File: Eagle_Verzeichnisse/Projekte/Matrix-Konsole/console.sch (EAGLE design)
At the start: 3 parts, among them IC1 74HC595N, IC2 74HC595N

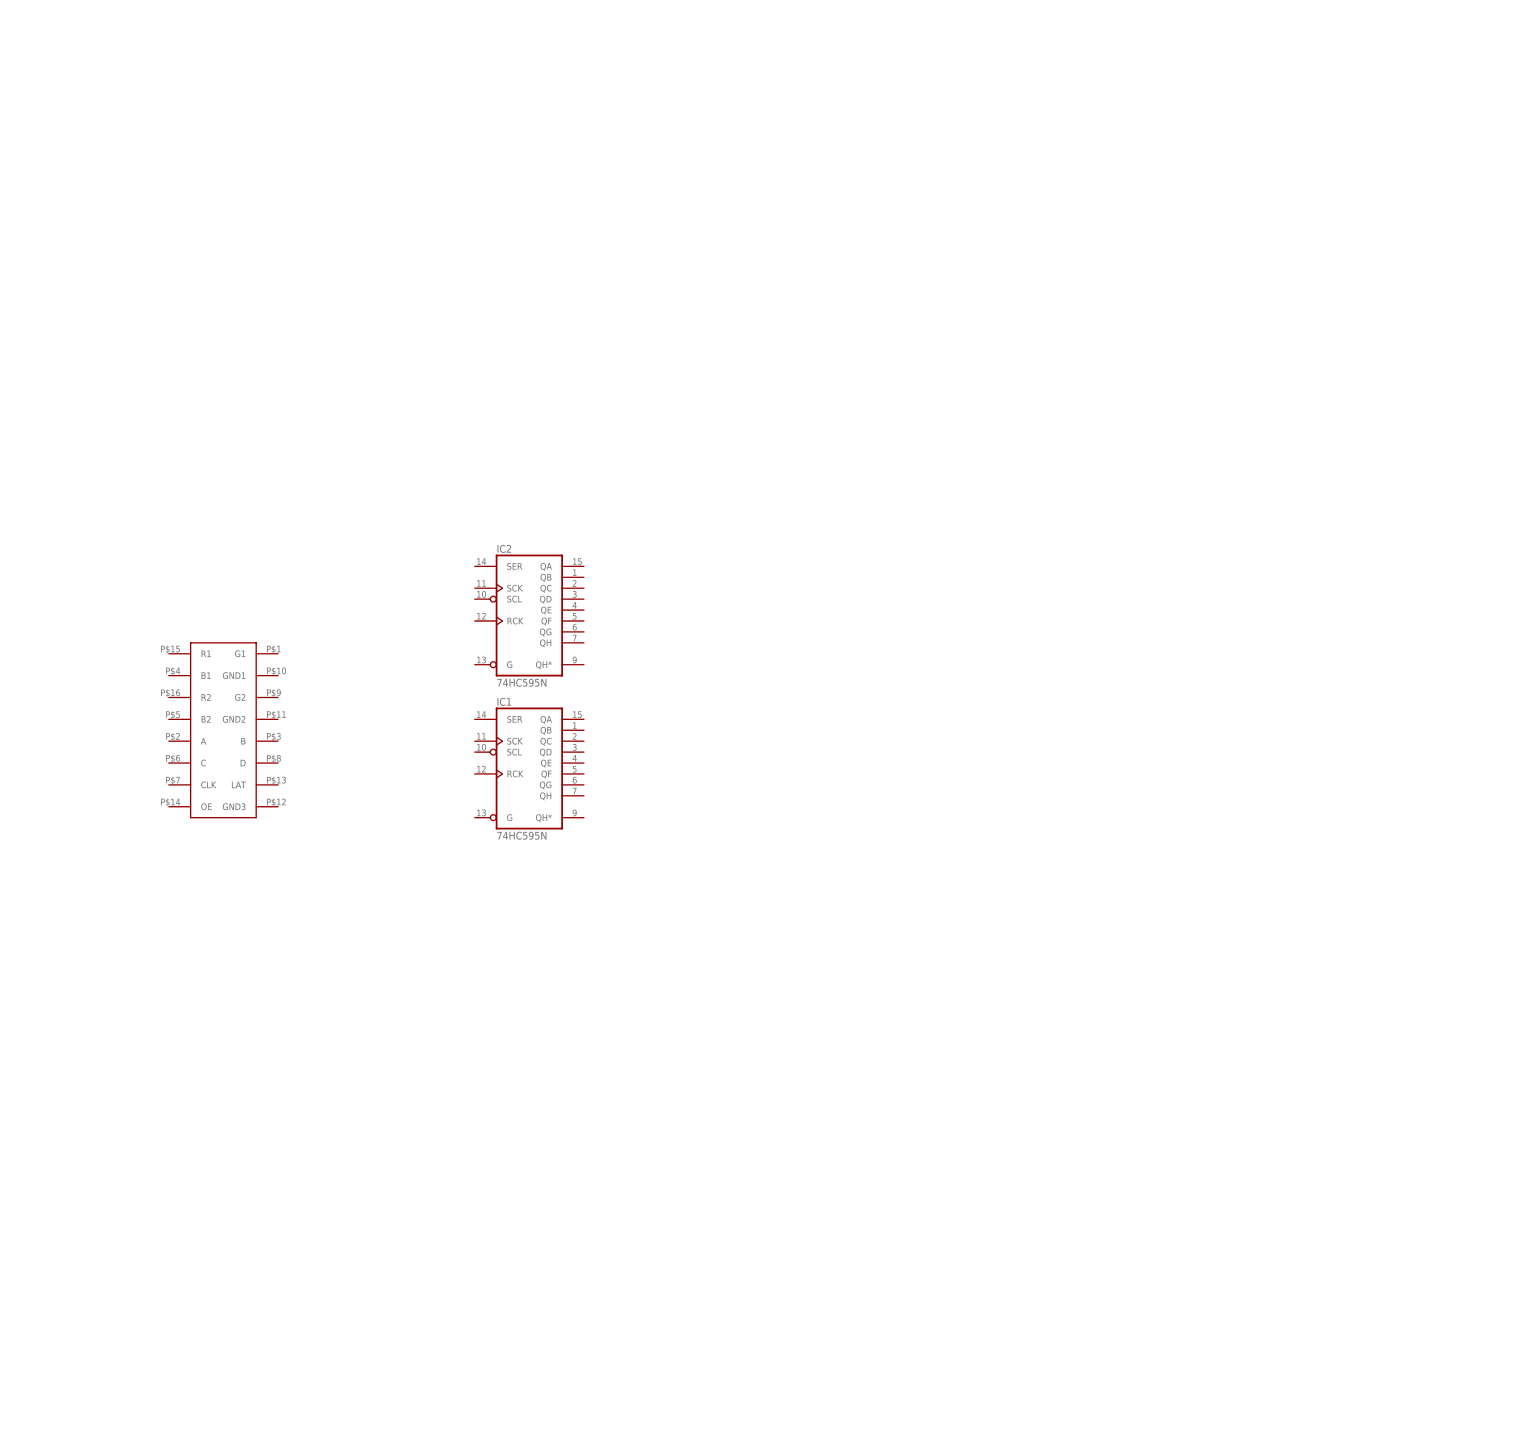
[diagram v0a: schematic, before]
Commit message: Added circuit diagrams, Changed Stückliste
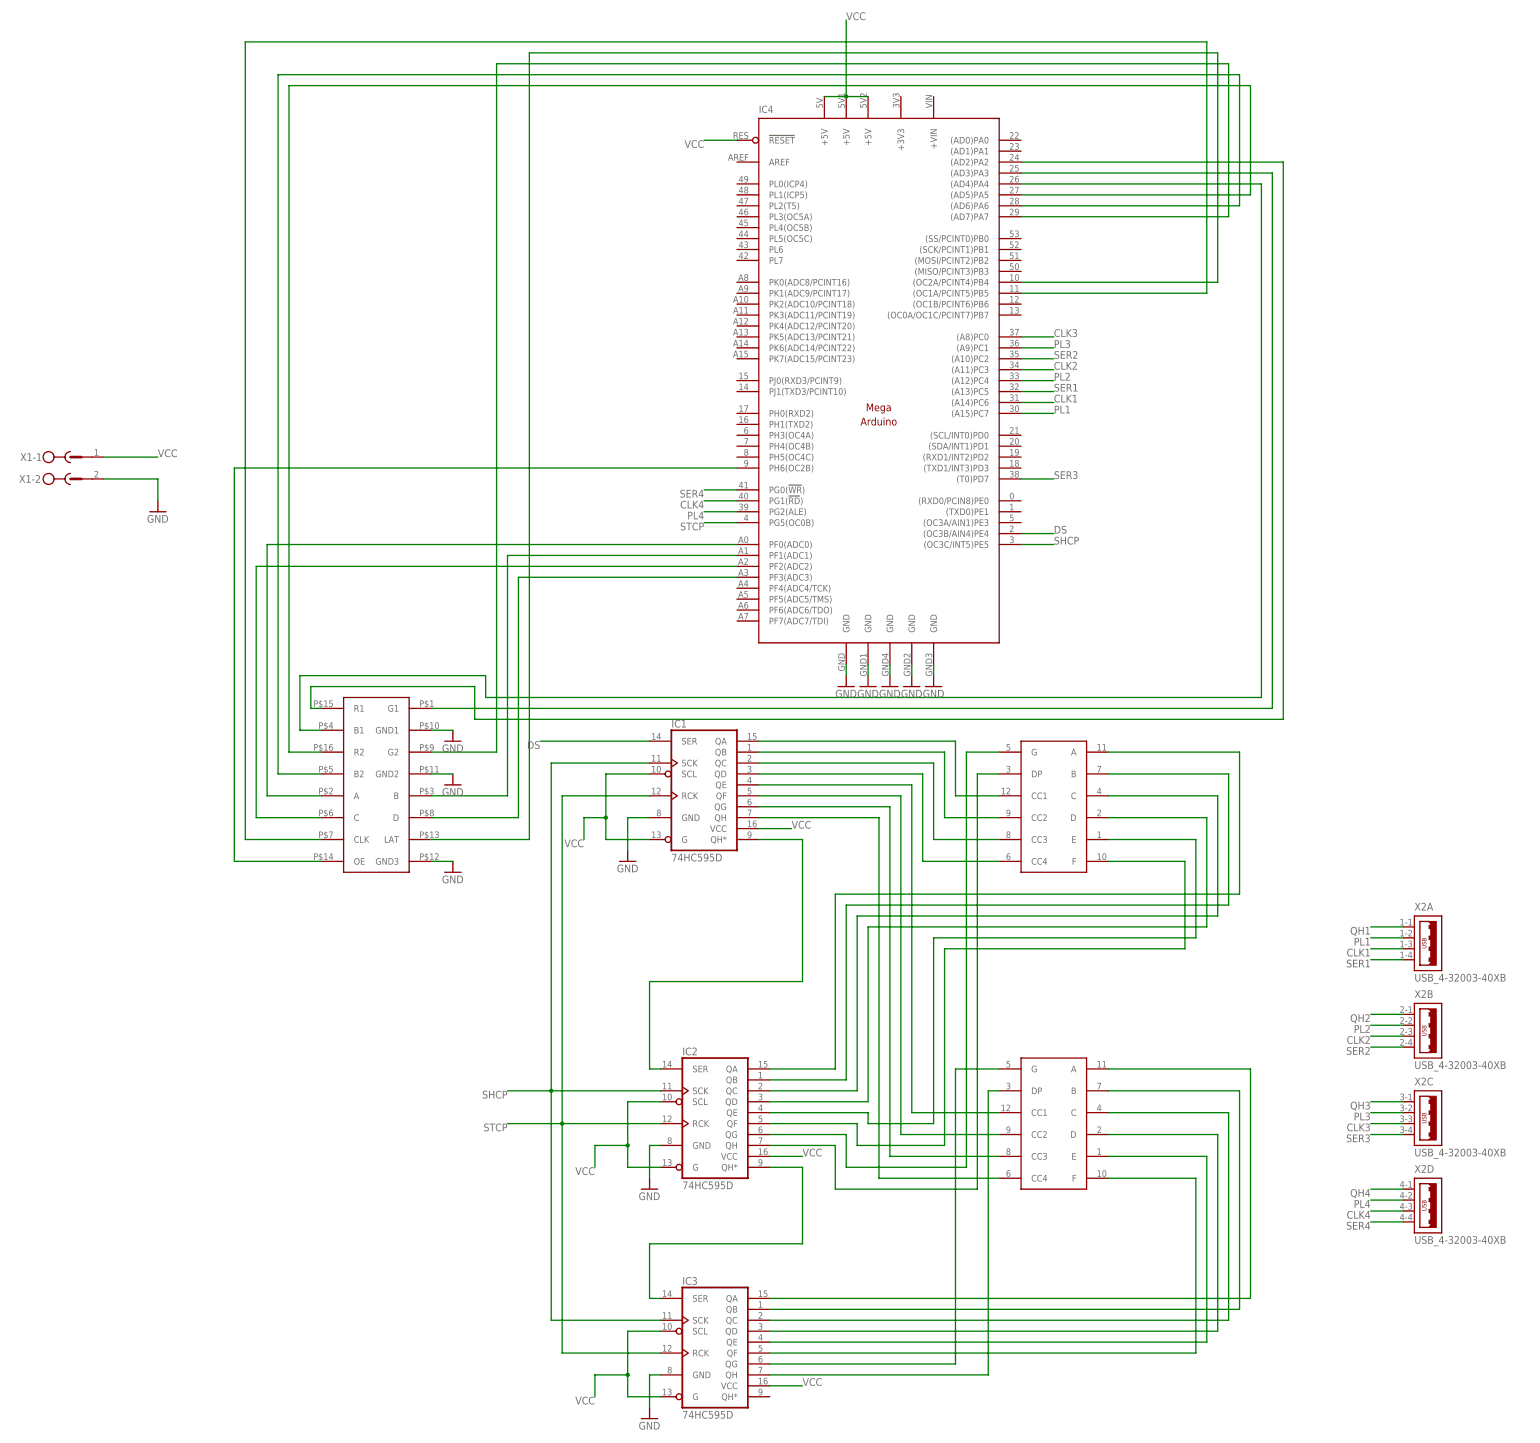
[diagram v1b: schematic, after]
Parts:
- added 7SEG1, 7SEG2: 7SEG_DEV, seven_segment:7SEG_DEV
- added IC3: 74HC595D, 74xx-eu:74HC595D
- added IC4: (no value), arduino:MEGAARDUINO_1
- added X1: (no value), con-phoenix-500:MSTBV2
- added X2: USB_4-32003-40XB, con-cypressindustries:USB_4-32003-40XB
- IC1, IC2: value 74HC595N -> 74HC595D; device 74xx-eu:74HC595N -> 74xx-eu:74HC595D
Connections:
- new net CLK1: IC4.(A14)PC6, X2A.3
- new net CLK2: IC4.(A11)PC3, X2B.3
- new net CLK3: IC4.(A8)PC0, X2C.3
- new net CLK4: IC4.PG1(!RD!), X2D.3
- new net DS: IC1.SER, IC4.(OC3B/AIN4)PE4
- new net GND: IC1.GND, IC2.GND, IC3.GND, IC4.GND@1, IC4.GND@2, IC4.GND@3, IC4.GND@4, IC4.GND@5, U$1.GND1, U$1.GND2, U$1.GND3, X1-2.SK
- new net N$1: IC4.(AD3)PA3, U$1.G1
- new net N$10: 7SEG2.CC4, IC1.QH
- new net N$11: 7SEG1.A, IC2.QA
- new net N$12: 7SEG1.B, IC2.QB
- new net N$13: 7SEG1.C, IC2.QC
- new net N$14: 7SEG1.D, IC2.QD
- new net N$15: 7SEG1.E, IC2.QE
- new net N$16: 7SEG1.F, IC2.QF
- new net N$17: 7SEG1.G, IC2.QG
- new net N$18: 7SEG1.DP, IC2.QH
- new net N$19: 7SEG2.A, IC3.QA
- new net N$2: IC4.(AD2)PA2, U$1.R1
- new net N$20: 7SEG2.B, IC3.QB
- new net N$21: 7SEG2.C, IC3.QC
- new net N$22: 7SEG2.D, IC3.QD
- new net N$23: 7SEG2.E, IC3.QE
- new net N$24: 7SEG2.F, IC3.QF
- new net N$25: 7SEG2.G, IC3.QG
- new net N$26: 7SEG2.DP, IC3.QH
- new net N$27: IC1.QH*, IC2.SER
- new net N$28: IC2.QH*, IC3.SER
- new net N$29: IC4.(AD4)PA4, U$1.B1
- new net N$3: 7SEG1.CC1, IC1.QA
- new net N$30: IC4.(AD5)PA5, U$1.R2
- new net N$31: IC4.(AD6)PA6, U$1.B2
- new net N$32: IC4.(AD7)PA7, U$1.G2
- new net N$33: IC4.PF0(ADC0), U$1.A
- new net N$34: IC4.PF1(ADC1), U$1.B
- new net N$35: IC4.PF2(ADC2), U$1.C
- new net N$36: IC4.PF3(ADC3), U$1.D
- new net N$37: IC4.(OC2A/PCINT4)PB4, U$1.LAT
- new net N$38: IC4.(OC1A/PCINT5)PB5, U$1.CLK
- new net N$39: IC4.PH6(OC2B), U$1.OE
- new net N$4: 7SEG1.CC2, IC1.QB
- new net N$5: 7SEG1.CC3, IC1.QC
- new net N$6: 7SEG1.CC4, IC1.QD
- new net N$7: 7SEG2.CC1, IC1.QE
- new net N$8: 7SEG2.CC2, IC1.QF
- new net N$9: 7SEG2.CC3, IC1.QG
- new net PL1: IC4.(A15)PC7, X2A.2
- new net PL2: IC4.(A12)PC4, X2B.2
- new net PL3: IC4.(A9)PC1, X2C.2
- new net PL4: IC4.PG2(ALE), X2D.2
- new net QH1: X2A.1
- new net QH2: X2B.1
- new net QH3: X2C.1
- new net QH4: X2D.1
- new net SER1: IC4.(A13)PC5, X2A.4
- new net SER2: IC4.(A10)PC2, X2B.4
- new net SER3: IC4.(T0)PD7, X2C.4
- new net SER4: IC4.PG0(!WR!), X2D.4
- new net SHCP: IC1.SCK, IC2.SCK, IC3.SCK, IC4.(OC3C/INT5)PE5
- new net STCP: IC1.RCK, IC2.RCK, IC3.RCK, IC4.PG5(OC0B)
- new net VCC: IC1.G, IC1.SCL, IC1.VCC, IC2.G, IC2.SCL, IC2.VCC, IC3.G, IC3.SCL, IC3.VCC, IC4.!RESET, IC4.+5V@1, IC4.+5V@2, IC4.+5V@3, X1-1.SK

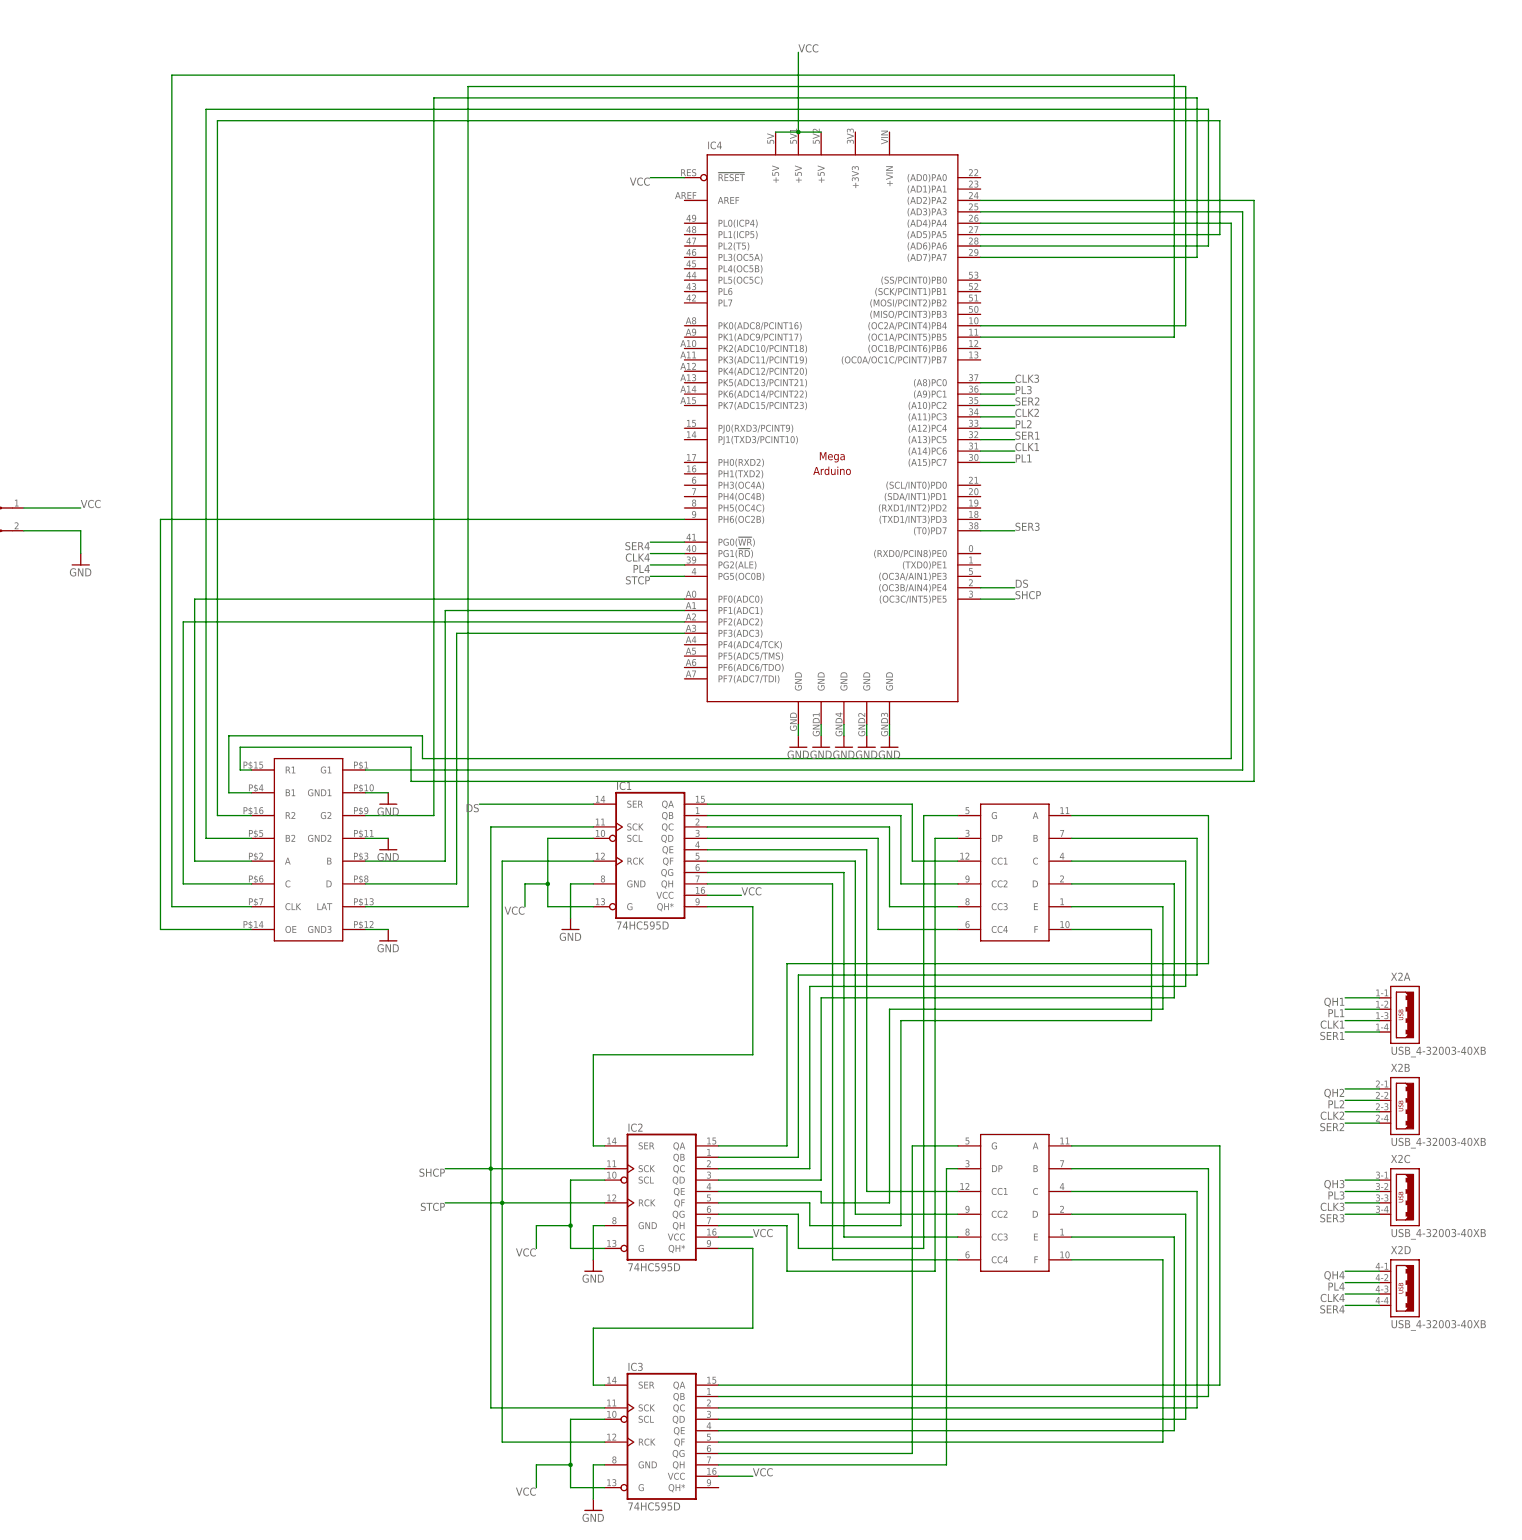
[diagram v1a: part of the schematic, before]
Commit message: Removed USB, Changed Labels
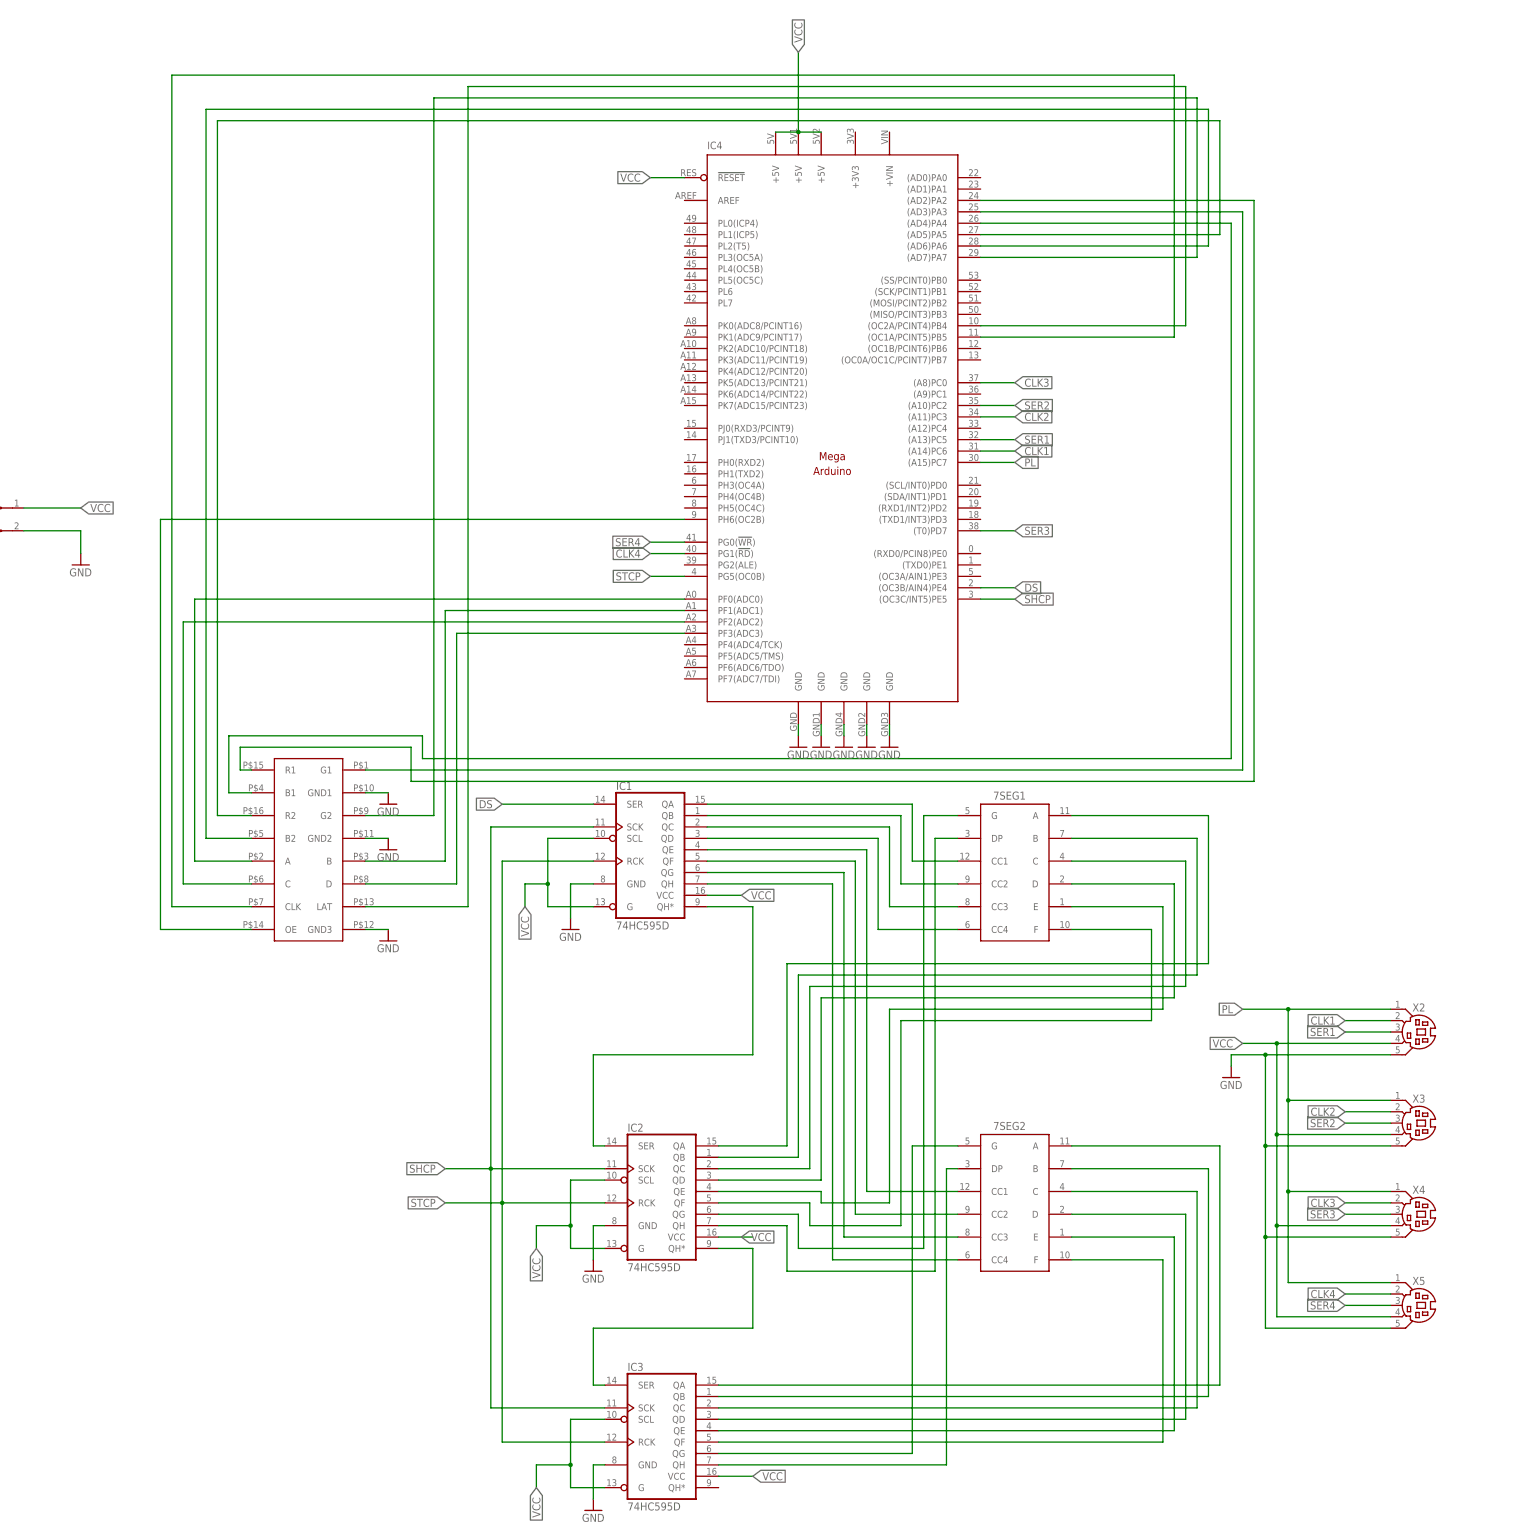
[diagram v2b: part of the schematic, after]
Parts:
- added X3, X4, X5: (no value), con-yamaichi:MDIN05K
- X2: value USB_4-32003-40XB -> (none); device con-cypressindustries:USB_4-32003-40XB -> con-yamaichi:MDIN05K
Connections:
- removed net PL1: IC4.(A15)PC7, X2A.2
- removed net PL2: IC4.(A12)PC4, X2B.2
- removed net PL3: IC4.(A9)PC1, X2C.2
- removed net PL4: IC4.PG2(ALE), X2D.2
- removed net QH1: X2A.1
- removed net QH2: X2B.1
- removed net QH3: X2C.1
- removed net QH4: X2D.1
- new net PL: IC4.(A15)PC7, X2.1, X3.1, X4.1, X5.1
- net CLK1: now also X2.2; no longer X2A.3
- net CLK2: now also X3.2; no longer X2B.3
- net CLK3: now also X4.2; no longer X2C.3
- net CLK4: now also X5.2; no longer X2D.3
- net GND: now also X2.5, X3.5, X4.5, X5.5
- net SER1: now also X2.3; no longer X2A.4
- net SER2: now also X3.3; no longer X2B.4
- net SER3: now also X4.3; no longer X2C.4
- net SER4: now also X5.3; no longer X2D.4
- net VCC: now also X2.4, X3.4, X4.4, X5.4
